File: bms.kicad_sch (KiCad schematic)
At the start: 83 parts, among them J1 Conn_01x13, J2 SWD, J3 I2C_IN, J4 I2C_OUT, U1 LMR51610, U2 STM32F103C8Tx, U3 MAX14920, U4 MAX11163, U5 MAX6126, U6 ADuM1252, Y1 8M

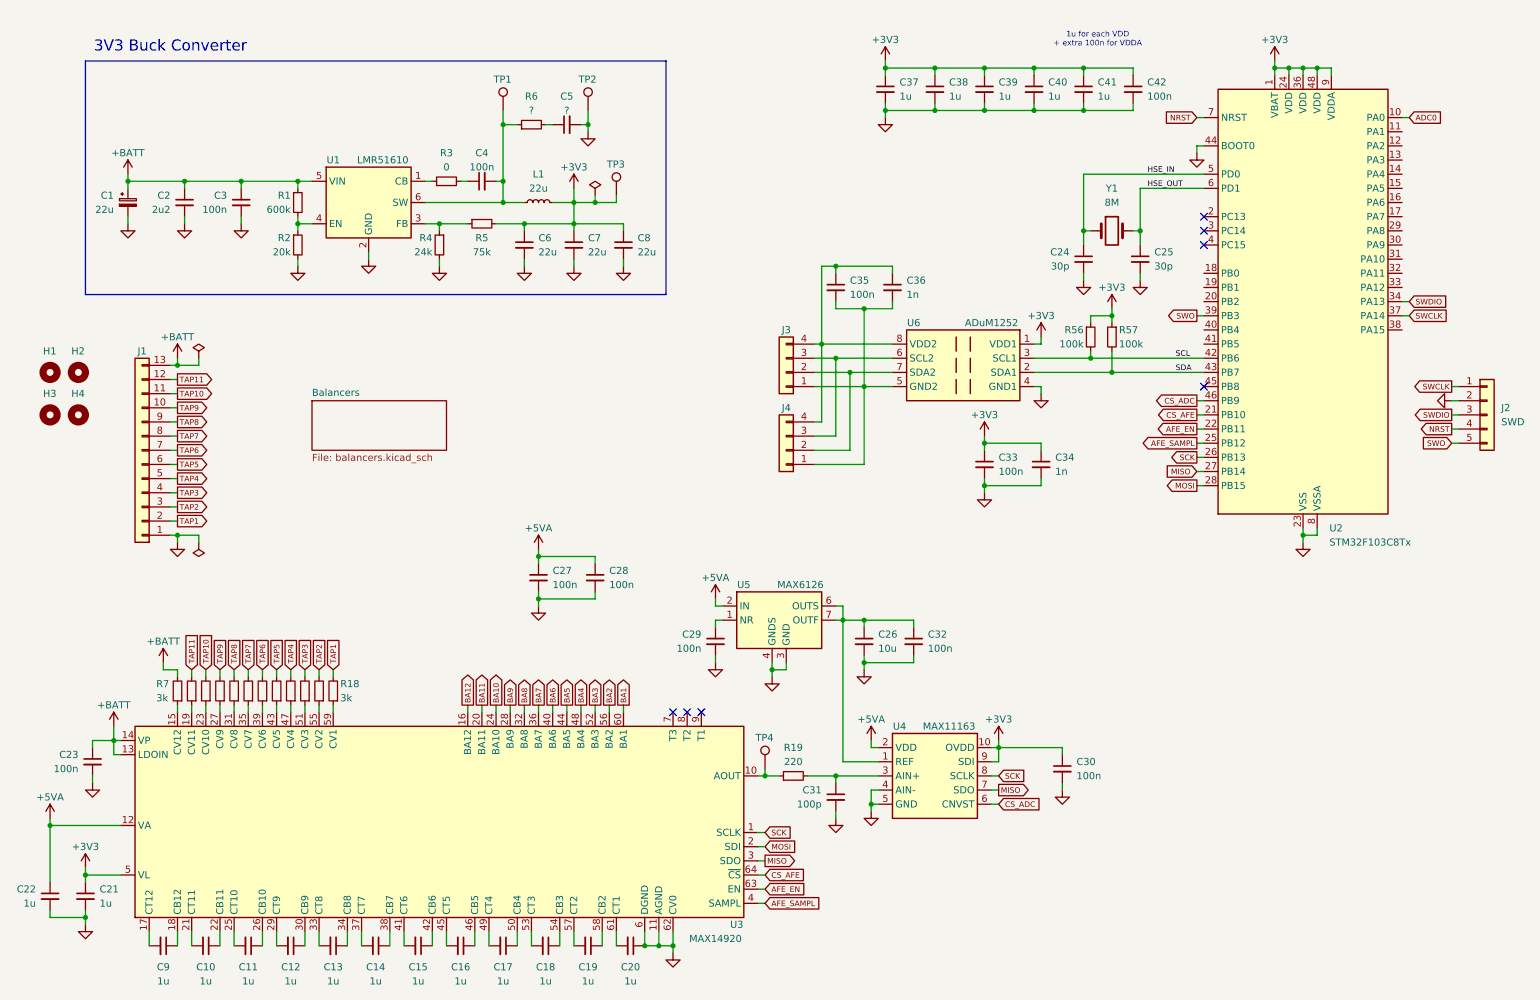
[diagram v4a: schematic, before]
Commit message: schematic: Add thermistors
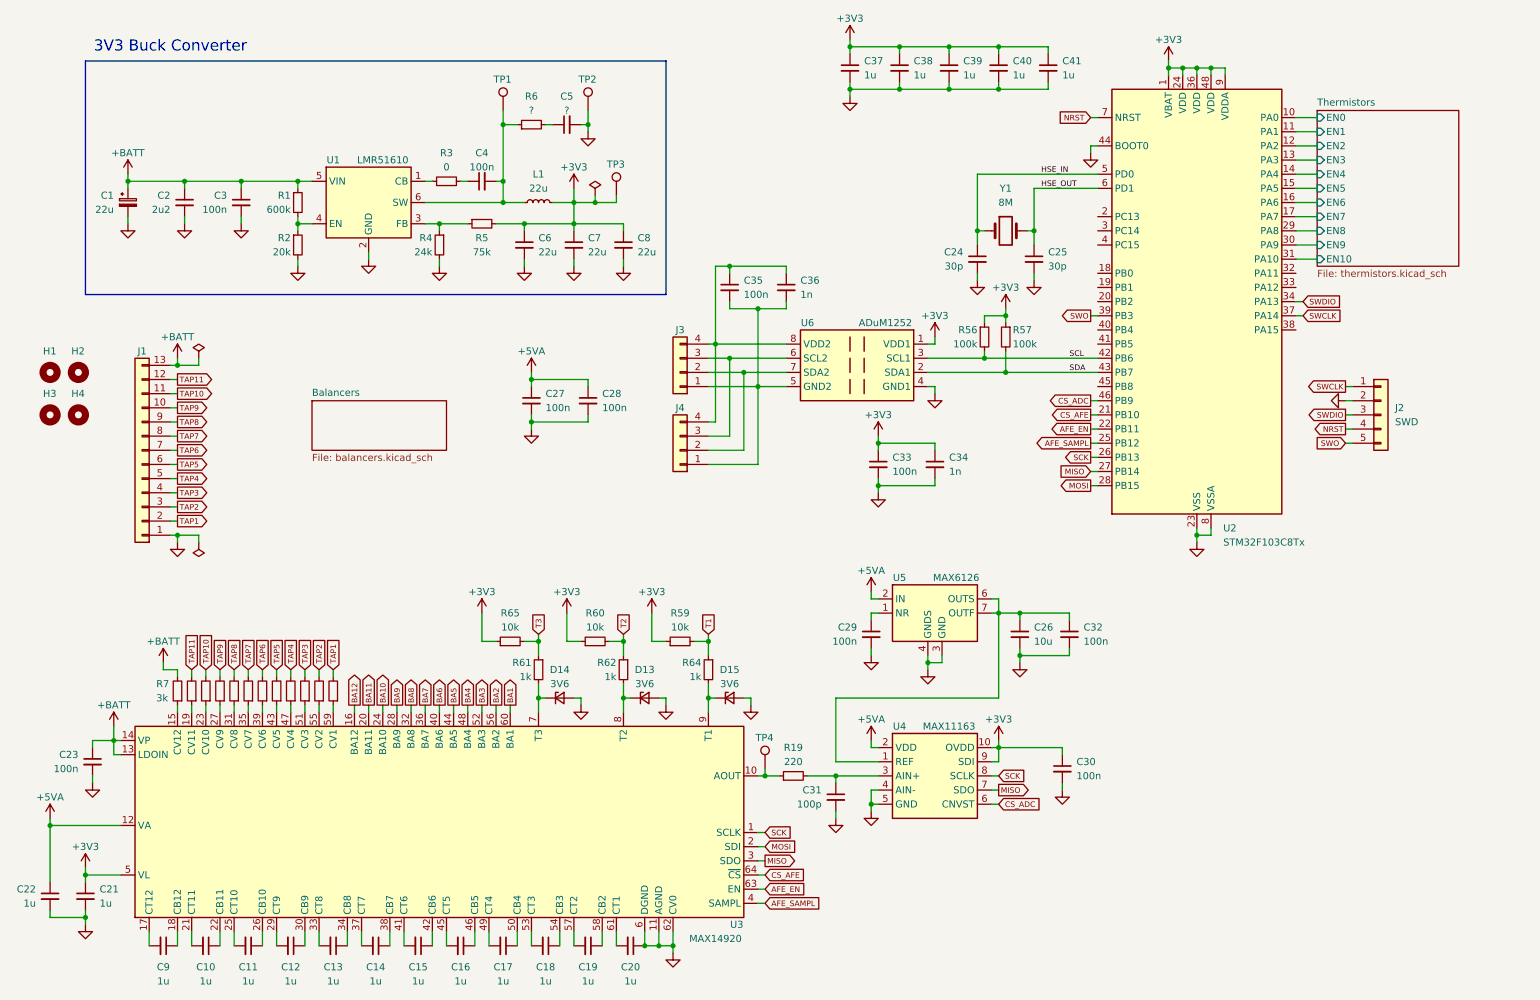
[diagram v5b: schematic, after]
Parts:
- removed C42: 100n, Capacitor_SMD:C_0603_1608Metric, symbol Device:C_Small
- added D13, D14, D15: 3V6, symbol Device:D_Zener_Small
- added R59, R60, R65: 10k, Resistor_SMD:R_0603_1608Metric, symbol Device:R_Small
- added R61, R62, R64: 1k, Resistor_SMD:R_0603_1608Metric, symbol Device:R_Small
- J1: Role (none) -> Cell tap connector
- J3, J4: footprint (none) -> Connector_JST:JST_PH_S4B-PH-K_1x04_P2.00mm_Horizontal; Part Number (none) -> S4B-PH-K-S
- R56: Role (none) -> I2C pull-up (SCL)
- R57: Role (none) -> I2C pull-up (SDA)
- U6: Role (none) -> I2C isolator
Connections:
- net +3V3: now also R59.1, R60.1, R65.1
- net GND: now also D13.2 (A), D14.2 (A), D15.2 (A)
- net Thermistors/EN1: now reaches U2.11 (PA1)
- net Thermistors/EN2: now reaches U2.12 (PA2)
- net Thermistors/EN3: now reaches U2.13 (PA3)
- net Thermistors/EN4: now reaches U2.14 (PA4)
- net Thermistors/EN5: now reaches U2.15 (PA5)
- net Thermistors/EN6: now reaches U2.16 (PA6)
- net Thermistors/EN7: now reaches U2.17 (PA7)
- net Thermistors/EN8: now reaches U2.29 (PA8)
- net Thermistors/EN9: now reaches U2.30 (PA9)
- net Thermistors/EN10: now reaches U2.31 (PA10)
- net at U3.7 (T3): now also D14.1 (K), R61.2
- net at U3.8 (T2): now also D13.1 (K), R62.2
- net at U3.9 (T1): now also D15.1 (K), R64.2
- net ADC0 renamed Thermistors/EN0
- new net T1: R59.2, R64.1
- new net T2: R60.2, R62.1
- new net T3: R61.1, R65.2
- no-connect marks 7 -> 0
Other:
- added sheet Thermistors (thermistors.kicad_sch)
- note removed: "1u for each VDD + extra 100n for VDDA"
- moved on the sheet: C24, C25, C26, C27, C28, C29, C32, C33, C34, C35, C36, C37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

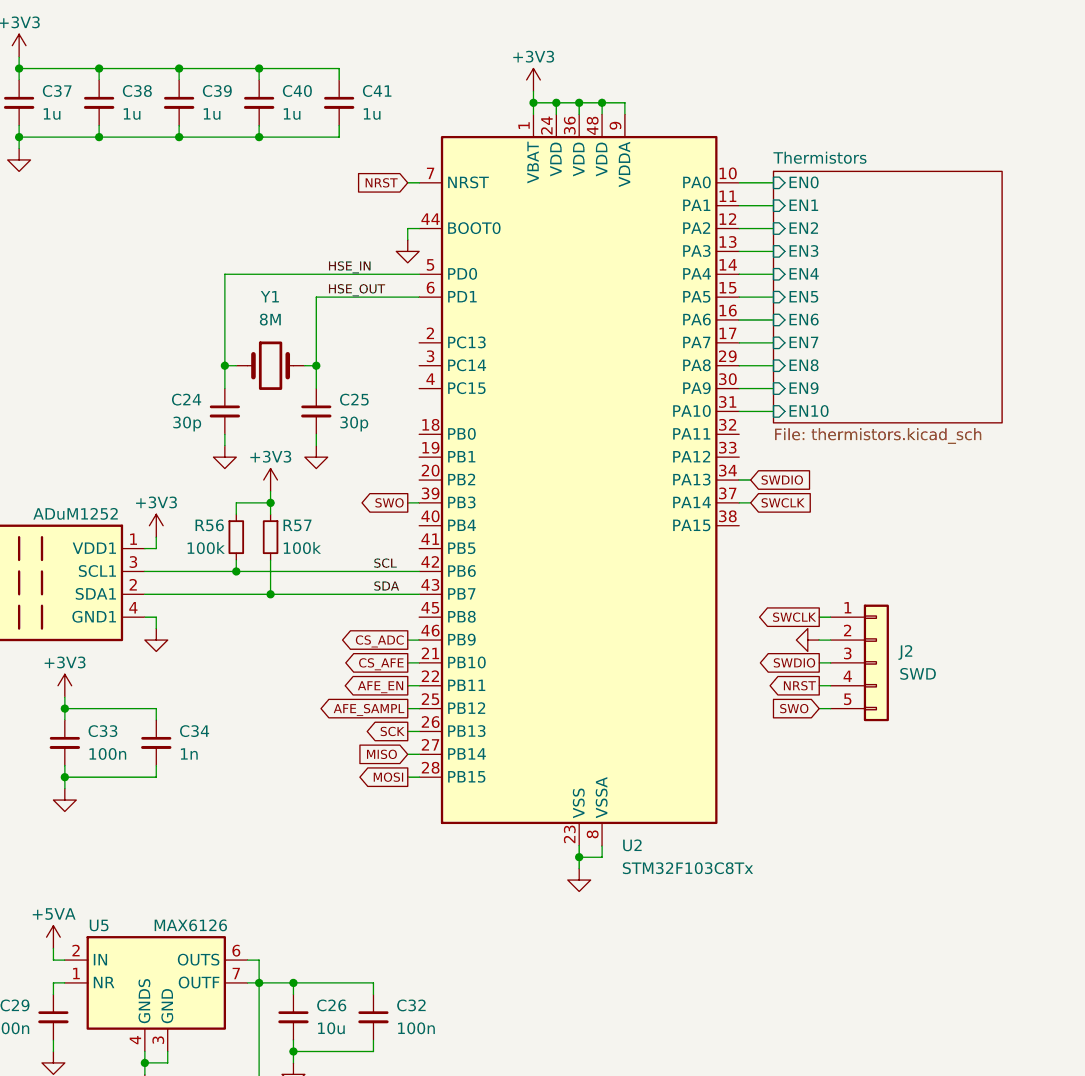
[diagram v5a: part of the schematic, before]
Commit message: schematic: MCU cleanup
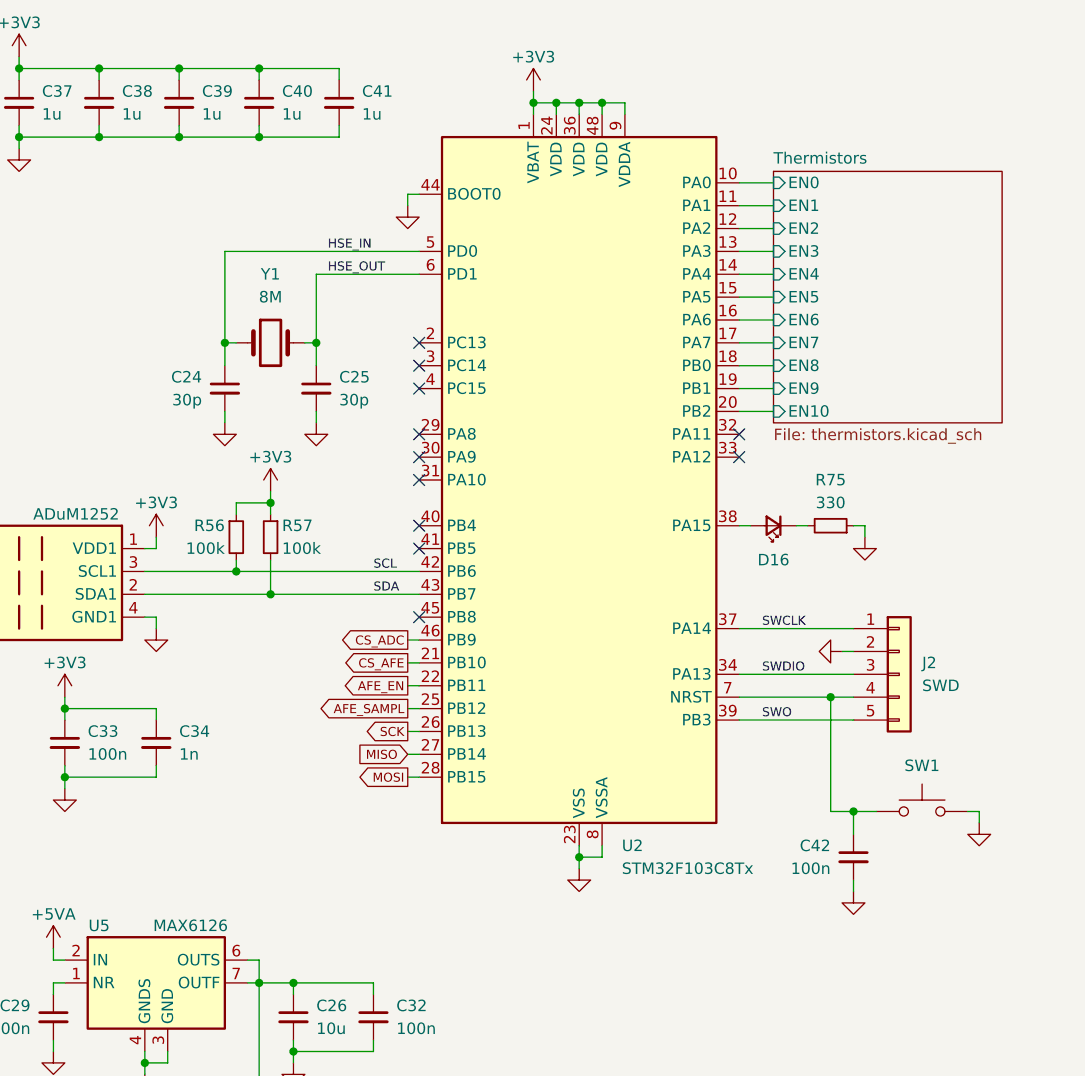
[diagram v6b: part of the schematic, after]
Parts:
- added C42: 100n, symbol Device:C_Small
- added D16: LED_Small, LED_SMD:LED_0603_1608Metric, symbol Device:LED_Small
- added R75: 330, Resistor_SMD:R_0603_1608Metric, symbol Device:R_Small
- added SW1: SW_Push, Button_Switch_SMD:SW_Push_SPST_NO_Alps_SKRK, symbol Switch:SW_Push
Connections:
- net GND: now also C42.2, R75.1, SW1.2
- net Thermistors/EN10: now also U2.20 (PB2); no longer U2.31 (PA10)
- net Thermistors/EN8: now also U2.18 (PB0); no longer U2.29 (PA8)
- net Thermistors/EN9: now also U2.19 (PB1); no longer U2.30 (PA9)
- net at U2.38 (PA15): now also D16.2 (A)
- net NRST: no longer names the net of J2.4 (Pin_4), U2.7 (NRST)
- net NRST: now also C42.1, SW1.1
- new net: D16.1 (K), R75.2
- no-connect marks 0 -> 11
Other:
- moved on the sheet: C24, C25, J2, Y1

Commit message: schematic: Assign inductor footprint and part number
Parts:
- C42: footprint (none) -> Capacitor_SMD:C_0603_1608Metric
- L1: footprint (none) -> Inductor_SMD:L_Vishay_IHLP-2525; Part Number (none) -> IHLP2525CZER220M1A
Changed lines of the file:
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@@
 			)
 		)
-		(property "Footprint" ""
+		(property "Footprint" "Capacitor_SMD:C_0603_1608Metric"
 			(at 255.27 109.22 0)
 			(effects
@@
 			)
 		)
-		(property "Footprint" ""
+		(property "Footprint" "Inductor_SMD:L_Vishay_IHLP-2525"
 			(at 106.68 49.53 0)
 			(effects
@@
 			)
 		)
-		(property "Part Number" ""
+		(property "Part Number" "IHLP2525CZER220M1A"
 			(at 106.68 49.53 0)
 			(effects

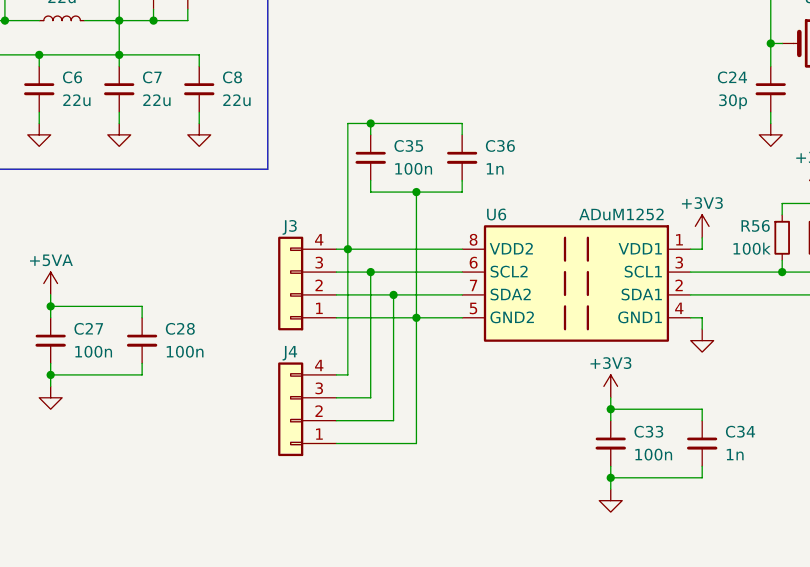
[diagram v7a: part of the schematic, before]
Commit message: schematic: Fix some pin types to make ERC happy
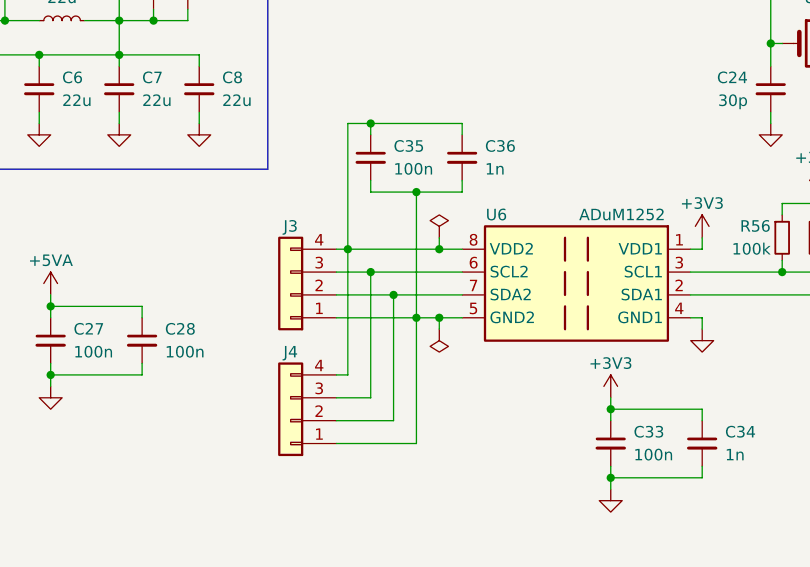
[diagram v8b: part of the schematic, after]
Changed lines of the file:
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@@
 	)
 	(junction
+		(at 148.59 82.55)
+		(diameter 0)
+		(color 0 0 0 0)
+	)
+	(junction
 		(at 189.23 123.19)
 		(diameter 0)
@@
 	)
 	(junction
+		(at 148.59 74.93)
+		(diameter 0)
+		(color 0 0 0 0)
+	)
+	(junction
 		(at 193.04 123.19)
 		(diameter 0)
@@
 	(wire
 		(pts
+			(xy 148.59 82.55) (xy 148.59 83.82)
+		)
+		(stroke
+			(width 0)
+			(type default)
+		)
+	)
+	(wire
+		(pts
 			(xy 166.37 120.65) (xy 167.64 120.65)
 		)
@@
 	(wire
 		(pts
+			(xy 148.59 73.66) (xy 148.59 74.93)
+		)
+		(stroke
+			(width 0)
+			(type default)
+		)
+	)
+	(wire
+		(pts
 			(xy 19.05 176.53) (xy 19.05 177.8)
 		)
@@
 	(wire
 		(pts
+			(xy 148.59 82.55) (xy 151.13 82.55)
+		)
+		(stroke
+			(width 0)
+			(type default)
+		)
+	)
+	(wire
+		(pts
 			(xy 205.74 100.33) (xy 207.01 100.33)
 		)
@@
 	(wire
 		(pts
-			(xy 138.43 74.93) (xy 151.13 74.93)
+			(xy 138.43 74.93) (xy 148.59 74.93)
 		)
 		(stroke
@@
 	(wire
 		(pts
-			(xy 146.05 82.55) (xy 151.13 82.55)
+			(xy 146.05 82.55) (xy 148.59 82.55)
 		)
 		(stroke
@@
 	(wire
 		(pts
+			(xy 148.59 74.93) (xy 151.13 74.93)
+		)
+		(stroke
+			(width 0)
+			(type default)
+		)
+	)
+	(wire
+		(pts
 			(xy 200.66 147.32) (xy 189.23 147.32)
 		)
@@
 	)
 	(symbol
+		(lib_id "power:PWR_FLAG")
+		(at 148.59 73.66 0)
+		(unit 1)
+		(exclude_from_sim no)
+		(in_bom yes)
+		(on_board yes)
+		(dnp no)
+		(fields_autoplaced yes)
+		(property "Reference" "#FLG04"
+			(at 148.59 71.755 0)
+			(effects
+				(font
+					(size 1.27 1.27)
+				)
+				(hide yes)
+			)
+		)
+		(property "Value" "PWR_FLAG"
+			(at 148.59 68.58 0)
+			(effects
+				(font
+					(size 1.27 1.27)
+				)
+				(hide yes)
+			)
+		)
+		(property "Footprint" ""
+			(at 148.59 73.66 0)
+			(effects
+				(font
+					(size 1.27 1.27)
+				)
+				(hide yes)
+			)
+		)
+		(property "Datasheet" "~"
+			(at 148.59 73.66 0)
+			(effects
+				(font
+					(size 1.27 1.27)
+				)
+				(hide yes)
+			)
+		)
+		(property "Description" "Special symbol for telling ERC where power comes from"
+			(at 148.59 73.66 0)
+			(effects
+				(font
+					(size 1.27 1.27)
+				)
+				(hide yes)
+			)
+		)
+		(pin "1"
+		)
+		(instances
+			(project "bms"
+				(path "/ae4a7653-8e6d-4e05-b144-1e5e3b2092b7"
+					(reference "#FLG04")
+					(unit 1)
+				)
+			)
+		)
+	)
+	(symbol
 		(lib_id "Device:R_Small")
 		(at 105.41 35.56 90)
@@
 					(unit 1)
 				)
+			)
+		)
+	)
+	(symbol
+		(lib_id "power:PWR_FLAG")
+		(at 148.59 83.82 180)
+		(unit 1)
+		(exclude_from_sim no)
+		(in_bom yes)
+		(on_board yes)
+		(dnp no)
+		(fields_autoplaced yes)
+		(property "Reference" "#FLG05"
+			(at 148.59 85.725 0)
+			(effects
+				(font
+					(size 1.27 1.27)
+				)
+				(hide yes)
+			)
+		)
+		(property "Value" "PWR_FLAG"
+			(at 148.59 88.9 0)
+			(effects
+				(font
+					(size 1.27 1.27)
+				)
+				(hide yes)
+			)
+		)
+		(property "Footprint" ""
+			(at 148.59 83.82 0)
+			(effects
+				(font
+					(size 1.27 1.27)
+				)
+				(hide yes)
+			)
+		)
+		(property "Datasheet" "~"
+			(at 148.59 83.82 0)
+			(effects
+				(font
+					(size 1.27 1.27)
+				)
+				(hide yes)
+			)
+		)
+		(property "Description" "Special symbol for telling ERC where power comes from"
+			(at 148.59 83.82 0)
+			(effects
+				(font
+					(size 1.27 1.27)
+				)
+				(hide yes)
+			)
+		)
+		(pin "1"
+		)
+		(instances
+			(project "bms"
+				(path "/ae4a7653-8e6d-4e05-b144-1e5e3b2092b7"
+					(reference "#FLG05")
+					(unit 1)
+				)
